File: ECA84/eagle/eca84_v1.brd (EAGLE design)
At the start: 223 x 127 mm, 184 parts

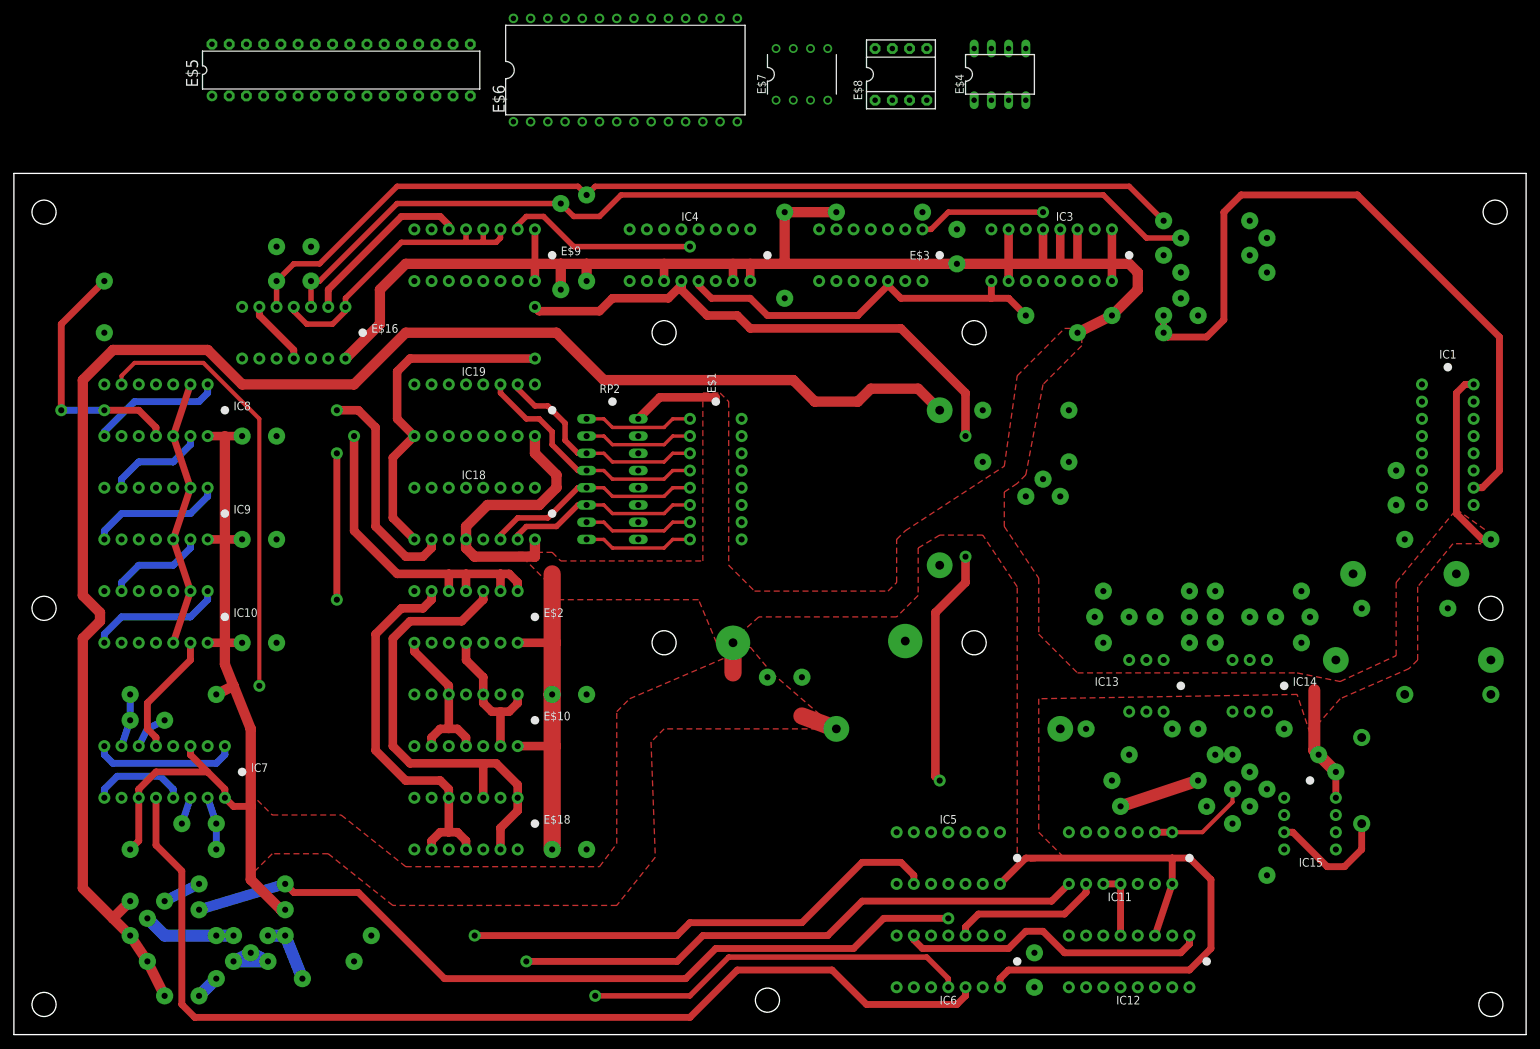
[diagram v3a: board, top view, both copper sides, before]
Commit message: Creando polígonos bottom
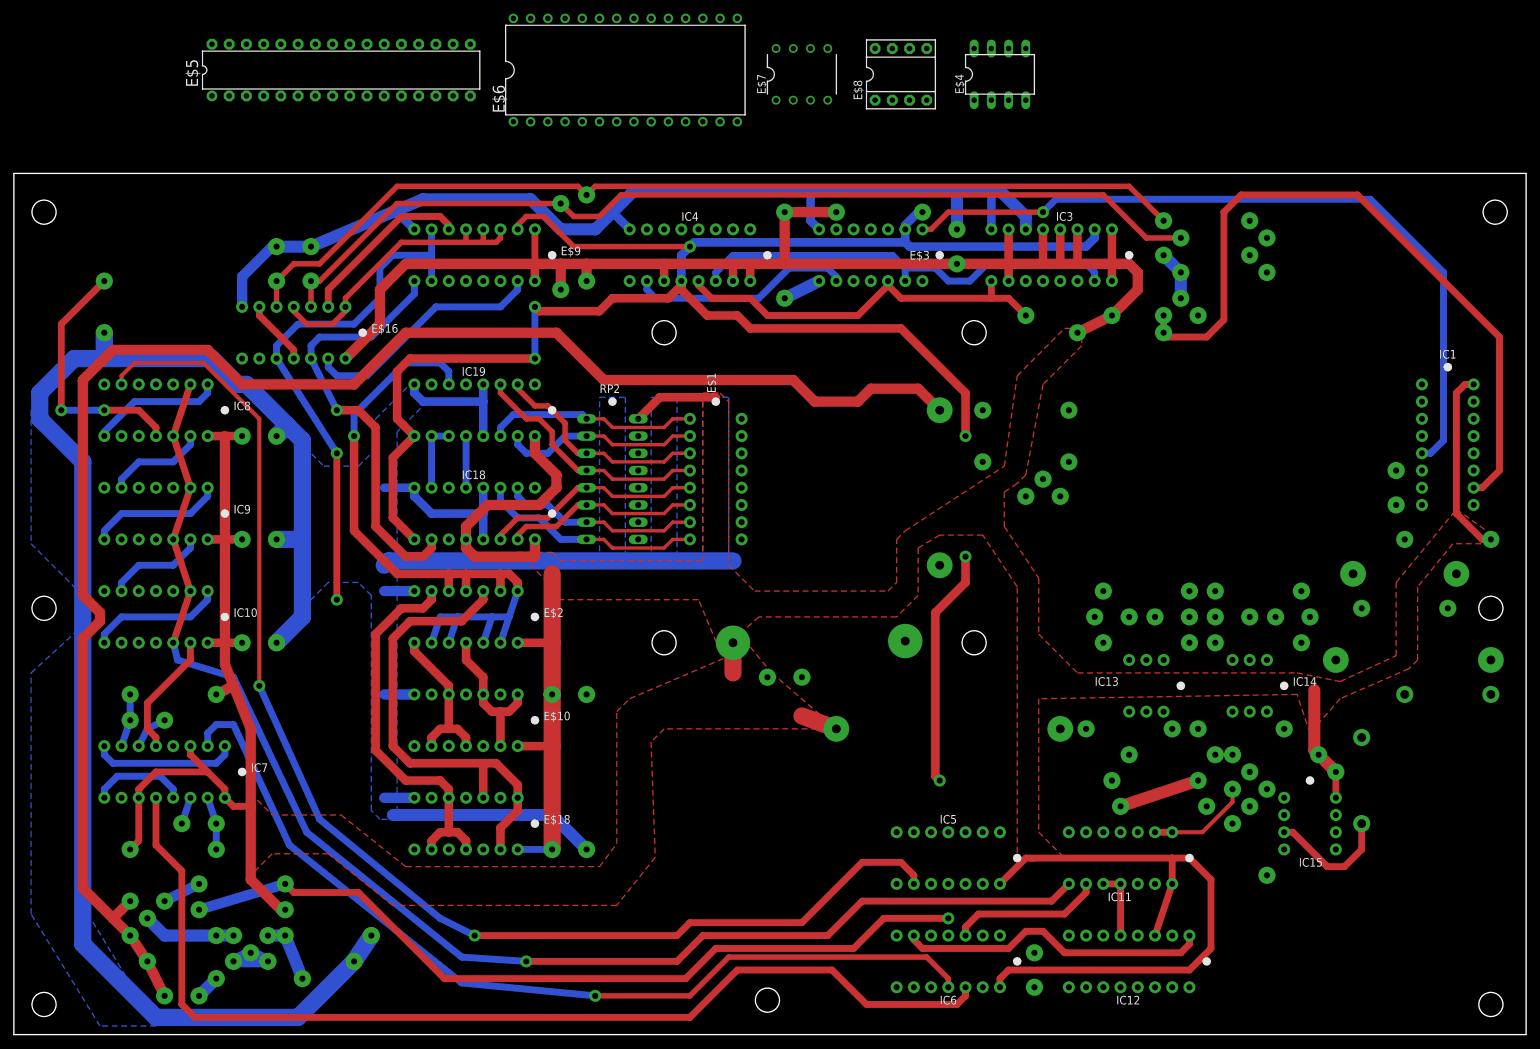
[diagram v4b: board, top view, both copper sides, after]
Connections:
- removed net S$63: E$12.P$1, E$21.P$1, E$23.P$1, E$25.P$1, E$50.P$1, E$51.P$1, IC8.P$7
- new net GND: E$10.P$7, E$12.P$1, E$18.P$7, E$2.P$7, E$21.P$1, E$23.P$1, E$25.P$1, E$50.P$1, E$51.P$1, E$92.P$1, IC18.P$13, IC18.P$4, IC18.P$8, IC19.P$13, IC19.P$4, IC19.P$8, IC8.P$7
- new net S$1: E$10.P$1, E$10.P$13, E$10.P$3, E$2.P$11
- new net S$14: E$103.P$1, E$117.P$1, E$143.P$1, E$161.P$1, E$163.P$1, E$77.P$1, IC1.P$8, IC1.P$9, IC13.P$4, IC5.P$7, IC6.P$7
- new net S$19: IC18.P$7, IC19.P$10, IC19.P$11
- new net S$20: E$74.P$1, E$75.P$1, E$76.P$1
- new net S$21: IC5.P$10, IC6.P$13, IC6.P$2, IC6.P$4
- new net S$25: IC5.P$8, IC6.P$5
- new net S$3: E$3.P$13, IC3.P$15, IC4.P$14
- new net S$36: E$14.P$1
- new net S$41: IC18.P$5, IC19.P$12
- net S$22: no longer E$10.P$1, E$10.P$13, E$10.P$3, E$2.P$11
- net S$29: now also IC18.P$2
- net S$31: now also IC19.P$14
- net S$32: now also IC19.P$15
- net S$34: now also IC18.P$3
- net S$42: now also IC1.P$5
- net S$7: now also IC5.P$11
- net VCC: now also E$18.P$14; no longer E$14.P$1
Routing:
- net GND: track 0.00 -> 363.3 mm
- net S$64: track 0.00 -> 156.5 mm
- net S$42: track 18.8 -> 111.9 mm
- net S$65: track 157.2 -> 238.3 mm
- net S$9: track 57.0 -> 135.2 mm
- net S$35: track 124.9 -> 200.3 mm
- net S$3: track 0.00 -> 64.5 mm
- net S$69: track 21.6 -> 78.7 mm
- net S$5: track 136.5 -> 186.8 mm
- net S$68: track 0.00 -> 36.3 mm
- net S$66: track 0.00 -> 32.7 mm
- net S$24: track 33.3 -> 64.0 mm
- net S$22: track 72.6 -> 103.1 mm
- net S$1: track 0.00 -> 22.4 mm
- net S$34: track 16.3 -> 33.3 mm
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- added copper zone on layer 16, net GND

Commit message: todos los conectores en lbr y pcb
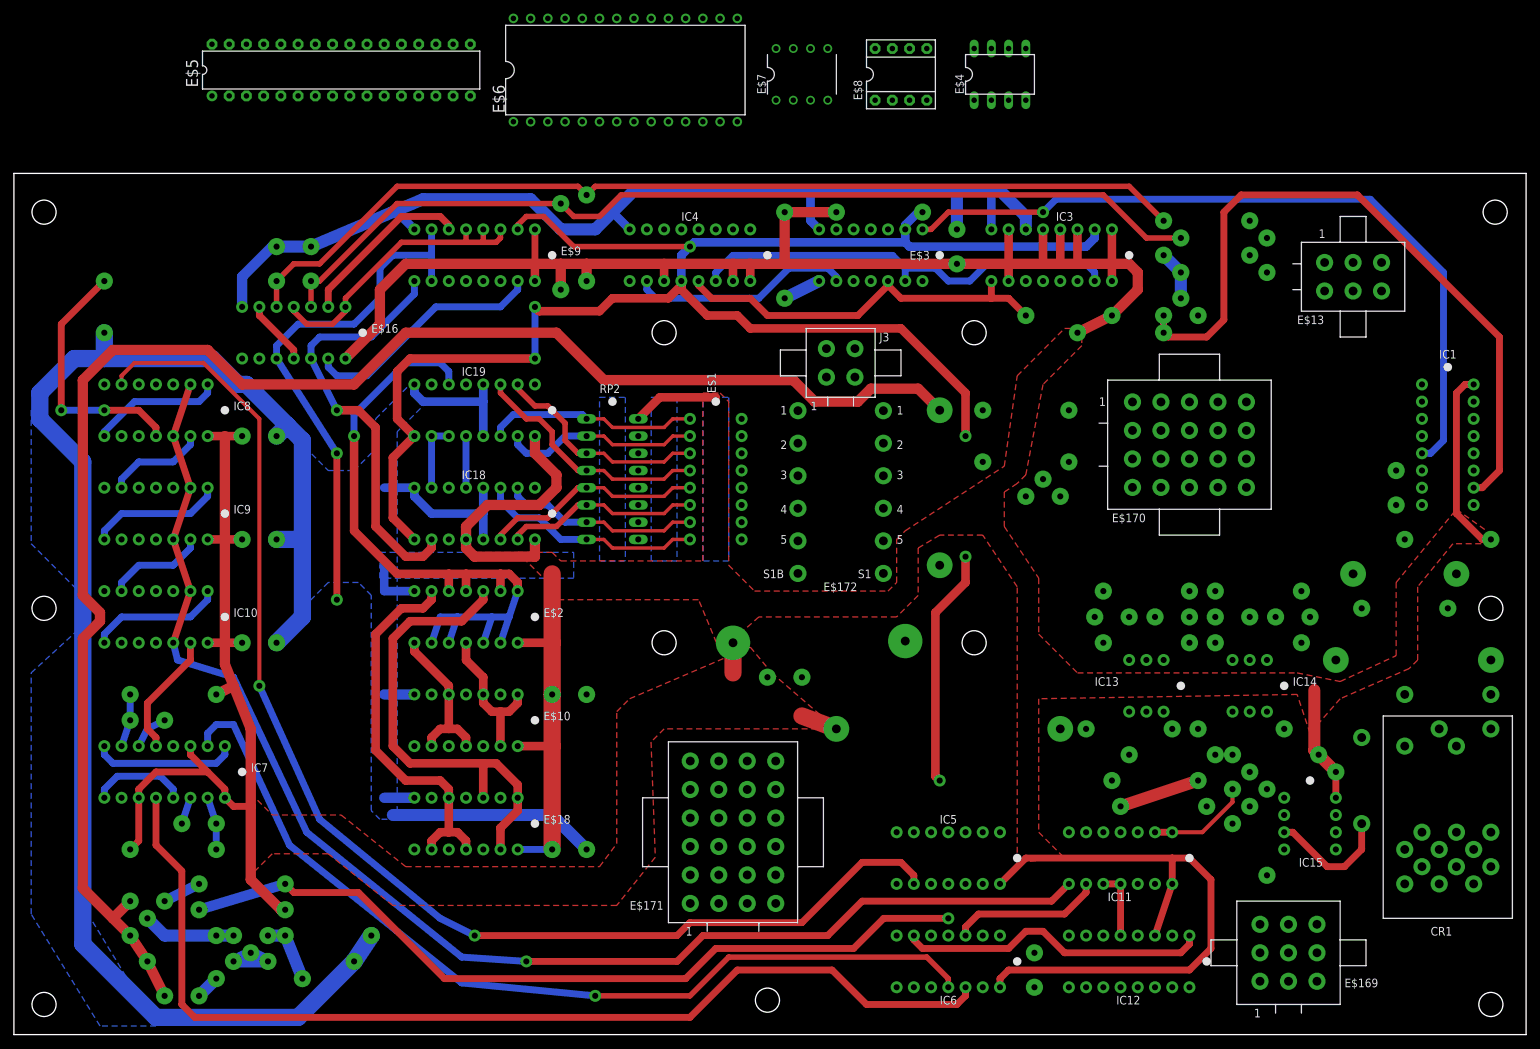
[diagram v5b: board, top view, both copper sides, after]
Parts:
- added CR1: (no value), eca84:CON-ZIGZAG
- added E$13: (no value), eca84:CON-2X3
- added E$169: (no value), eca84:CON-3X3
- added E$170: (no value), eca84:CON-4X5
- added E$171: (no value), eca84:CON-4X6
- added E$172: (no value), eca84:CON-2X6
- added J3: (no value), eca84:CON-2X2
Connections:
- new net S$63: IC18.P$13, IC18.P$4, IC18.P$8, IC19.P$13, IC19.P$4, IC19.P$8
- net GND: no longer IC18.P$13, IC18.P$4, IC18.P$8, IC19.P$13, IC19.P$4, IC19.P$8
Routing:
- net GND: track 363.3 -> 271.3 mm
- net S$63: track 0.00 -> 44.1 mm
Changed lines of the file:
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@@
 <setting verticaltext="up"/>
 </settings>
-<grid distance="25" unitdist="mil" unit="mil" style="lines" multiple="1" display="yes" altdistance="25" altunitdist="mil" altunit="mil"/>
+<grid distance="50" unitdist="mil" unit="mil" style="lines" multiple="1" display="yes" altdistance="25" altunitdist="mil" altunit="mil"/>
 <layers>
-<layer number="1" name="Top" color="4" fill="1" visible="no" active="yes"/>
+<layer number="1" name="Top" color="4" fill="1" visible="yes" active="yes"/>
 <layer number="2" name="Route2" color="16" fill="1" visible="no" active="no"/>
 <layer number="3" name="Route3" color="17" fill="1" visible="no" active="no"/>
@@
 <element name="E$167" library="eca84" package="ROUND-6" value="" x="106.045" y="57.785" smashed="yes"/>
 <element name="E$168" library="eca84" package="ROUND-3" value="" x="113.665" y="108.585" smashed="yes"/>
+<element name="CR1" library="eca84" package="CON-ZIGZAG" value="" x="211.455" y="33.655" smashed="yes">
+<attribute name="NAME" x="208.915" y="14.605" size="1.27" layer="25"/>
+</element>
+<element name="J3" library="eca84" package="CON-2X2" value="" x="121.92" y="99.06" smashed="yes">
+<attribute name="NAME" x="127.635" y="102.235" size="1.27" layer="25"/>
+</element>
+<element name="E$13" library="eca84" package="CON-2X3" value="" x="197.485" y="111.76" smashed="yes">
+<attribute name="NAME" x="189.23" y="104.775" size="1.27" layer="25"/>
+</element>
+<element name="E$169" library="eca84" package="CON-3X3" value="" x="187.96" y="12.065" smashed="yes">
+<attribute name="NAME" x="196.215" y="6.985" size="1.27" layer="25"/>
+</element>
+<element name="E$170" library="eca84" package="CON-4X5" value="" x="173.355" y="86.995" smashed="yes">
+<attribute name="NAME" x="161.925" y="75.565" size="1.27" layer="25"/>
+</element>
+<element name="E$171" library="eca84" package="CON-4X6" value="" x="106.045" y="29.845" smashed="yes">
+<attribute name="NAME" x="90.805" y="18.415" size="1.27" layer="25"/>
+</element>
+<element name="E$172" library="eca84" package="CON-2X6" value="" x="121.92" y="80.01" smashed="yes">
+<attribute name="NAME" x="119.38" y="65.405" size="1.27" layer="25"/>
+</element>
 </elements>
 <signals>
@@
 <wire x1="29.845" y1="8.255" x2="27.305" y2="5.715" width="1.778" layer="16"/>
 </signal>
+<signal name="S$63">
+<contactref element="IC19" pad="P$8"/>
+<wire x1="59.055" y1="94.615" x2="59.055" y2="95.885" width="1.27" layer="16"/>
+<wire x1="60.325" y1="93.345" x2="59.055" y2="94.615" width="1.27" layer="16"/>
+<contactref element="IC19" pad="P$4"/>
+<wire x1="69.215" y1="95.885" x2="69.215" y2="93.345" width="1.27" layer="16"/>
+<wire x1="69.215" y1="93.345" x2="60.325" y2="93.345" width="1.27" layer="16"/>
+<contactref element="IC19" pad="P$13"/>
+<wire x1="69.215" y1="88.265" x2="69.215" y2="93.345" width="1.27" layer="16"/>
+<contactref element="IC18" pad="P$13"/>
+<contactref element="IC18" pad="P$4"/>
+<wire x1="69.215" y1="80.645" x2="69.215" y2="76.835" width="1.27" layer="16"/>
+<wire x1="69.215" y1="76.835" x2="69.215" y2="73.025" width="1.27" layer="16"/>
+<wire x1="61.595" y1="76.835" x2="69.215" y2="76.835" width="1.27" layer="16"/>
+<wire x1="59.055" y1="79.375" x2="61.595" y2="76.835" width="1.27" layer="16"/>
+<contactref element="IC18" pad="P$8"/>
+<wire x1="59.055" y1="80.645" x2="59.055" y2="79.375" width="1.27" layer="16"/>
+<wire x1="54.61" y1="80.645" x2="59.055" y2="80.645" width="1.27" layer="16"/>
+<wire x1="69.215" y1="80.645" x2="69.215" y2="88.265" width="0" layer="19" extent="1-1"/>
+</signal>
 <signal name="GND">
 <contactref element="E$50" pad="P$1"/>
@@
 <wire x1="3.81" y1="94.615" x2="3.81" y2="90.805" width="2.54" layer="16"/>
 <wire x1="52.705" y1="14.605" x2="50.165" y2="10.795" width="2.54" layer="16"/>
-<contactref element="E$18" pad="P$7"/>
-<contactref element="E$92" pad="P$1"/>
-<contactref element="E$10" pad="P$7"/>
-<contactref element="E$2" pad="P$7"/>
-<contactref element="IC19" pad="P$8"/>
-<contactref element="IC19" pad="P$4"/>
-<contactref element="IC19" pad="P$13"/>
 <polygon width="0.254" layer="16" thermals="no">
 <vertex x="41.91" y="87.63"/>
-<vertex x="45.72" y="83.82"/>
-<vertex x="50.8" y="83.82"/>
+<vertex x="46.355" y="83.185"/>
+<vertex x="50.165" y="83.185"/>
 <vertex x="53.34" y="86.36"/>
 <vertex x="53.34" y="90.805"/>
@@
 <vertex x="2.54" y="53.34"/>
 </polygon>
-<wire x1="59.055" y1="50.165" x2="54.61" y2="50.165" width="1.524" layer="16"/>
-<wire x1="59.055" y1="65.405" x2="54.61" y2="65.405" width="1.524" layer="16"/>
-<wire x1="59.055" y1="34.925" x2="54.61" y2="34.925" width="1.524" layer="16"/>
-<contactref element="IC18" pad="P$4"/>
-<contactref element="IC18" pad="P$13"/>
-<contactref element="IC18" pad="P$8"/>
-<wire x1="69.215" y1="80.645" x2="69.215" y2="76.835" width="1.27" layer="16"/>
-<wire x1="69.215" y1="76.835" x2="69.215" y2="73.025" width="1.27" layer="16"/>
-<wire x1="59.055" y1="80.645" x2="59.055" y2="79.375" width="1.27" layer="16"/>
-<wire x1="59.055" y1="79.375" x2="61.595" y2="76.835" width="1.27" layer="16"/>
-<wire x1="61.595" y1="76.835" x2="69.215" y2="76.835" width="1.27" layer="16"/>
-<wire x1="59.055" y1="80.645" x2="54.61" y2="80.645" width="1.27" layer="16"/>
-<wire x1="69.215" y1="95.885" x2="69.215" y2="93.345" width="1.27" layer="16"/>
-<wire x1="69.215" y1="88.265" x2="69.215" y2="93.345" width="1.27" layer="16"/>
-<wire x1="69.215" y1="93.345" x2="60.325" y2="93.345" width="1.27" layer="16"/>
-<wire x1="60.325" y1="93.345" x2="59.055" y2="94.615" width="1.27" layer="16"/>
-<wire x1="59.055" y1="94.615" x2="59.055" y2="95.885" width="1.27" layer="16"/>
-<wire x1="84.455" y1="27.305" x2="79.375" y2="32.385" width="1.778" layer="16"/>
-<wire x1="79.375" y1="32.385" x2="55.88" y2="32.385" width="1.778" layer="16"/>
-<polygon width="0.254" layer="16">
+<polygon width="0.254" layer="16" thermals="no">
 <vertex x="86.36" y="93.98"/>
 <vertex x="90.17" y="93.98"/>
@@
 <vertex x="86.36" y="69.85"/>
 </polygon>
-<polygon width="0.254" layer="16">
+<polygon width="0.254" layer="16" thermals="no">
 <vertex x="93.98" y="93.98"/>
 <vertex x="97.79" y="93.98"/>
@@
 <vertex x="93.98" y="69.85"/>
 </polygon>
-<polygon width="0.254" layer="16">
+<polygon width="0.254" layer="16" thermals="no">
 <vertex x="101.6" y="93.98"/>
 <vertex x="105.41" y="93.98"/>
@@
 <vertex x="101.6" y="69.85"/>
 </polygon>
-<wire x1="54.61" y1="69.215" x2="55.245" y2="69.85" width="2.54" layer="16"/>
-<wire x1="55.245" y1="69.85" x2="106.045" y2="69.85" width="2.54" layer="16"/>
+<contactref element="E$92" pad="P$1"/>
+<contactref element="E$2" pad="P$7"/>
+<wire x1="59.055" y1="65.405" x2="54.61" y2="65.405" width="1.27" layer="16"/>
+<contactref element="E$10" pad="P$7"/>
+<wire x1="59.055" y1="50.165" x2="54.61" y2="50.165" width="1.524" layer="16"/>
+<wire x1="84.455" y1="27.305" x2="79.375" y2="32.385" width="1.778" layer="16"/>
+<wire x1="79.375" y1="32.385" x2="55.88" y2="32.385" width="1.778" layer="16"/>
+<contactref element="E$18" pad="P$7"/>
+<wire x1="59.055" y1="34.925" x2="54.61" y2="34.925" width="1.524" layer="16"/>
+<polygon width="0.254" layer="16" thermals="no">
+<vertex x="53.975" y="71.12"/>
+<vertex x="82.55" y="71.12"/>
+<vertex x="82.55" y="67.31"/>
+<vertex x="53.975" y="67.31"/>
+</polygon>
+<wire x1="54.61" y1="65.405" x2="54.61" y2="69.215" width="1.27" layer="16"/>
 <wire x1="13.335" y1="103.505" x2="13.335" y2="95.885" width="0" layer="19" extent="1-1"/>
 </signal>

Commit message: terminado pistas top
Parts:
- removed E$4: (no value), 40xx:DIL08
- removed E$5: (no value), am29-memory:DIL32-3
- removed E$6: (no value), analog-devices:DIL28-6
- removed E$7: (no value), avago:DIL08
- removed E$8: (no value), burr-brown:DIL08
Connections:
- new net S$70: E$1.P$11, E$172.P$4
- new net S$71: E$1.P$10, E$172.P$6
- new net S$72: E$1.P$9, E$172.P$10
- new net S$73: E$141.P$1, E$170.P$9
- new net S$74: E$140.P$1, E$170.P$13
- new net S$75: E$13.P$2, E$170.P$17
- new net S$76: E$13.P$1, E$170.P$14
- new net S$77: E$170.P$10, E$85.P$1
- new net S$78: E$170.P$11, E$89.P$1
- new net S$79: E$13.P$3, E$162.P$1
- net S$36: now also E$1.P$12, E$172.P$2; no longer E$14.P$1
- net VCC: now also E$14.P$1, IC1.P$11
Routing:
- net S$79: track 0.00 -> 47.6 mm
- net S$74: track 0.00 -> 37.0 mm
- net S$73: track 0.00 -> 30.4 mm
- net S$76: track 0.00 -> 30.2 mm
- net S$70: track 0.00 -> 24.7 mm
- net S$71: track 0.00 -> 24.1 mm
- net S$72: track 0.00 -> 23.0 mm
- net S$78: track 0.00 -> 21.3 mm
- net S$36: track 5.43 -> 25.6 mm
- net S$75: track 0.00 -> 20.0 mm
- net S$77: track 0.00 -> 19.0 mm
- net VCC: track 491.7 -> 499.6 mm

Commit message: Antes de cambiar angulo de pistas
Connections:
- new net S$80: E$10.P$6, E$171.P$20
- new net S$81: E$10.P$4, E$171.P$24
- new net S$82: E$10.P$2, E$171.P$16
- new net S$83: E$10.P$10, E$171.P$17
- new net S$84: E$10.P$12, E$171.P$13
- new net S$85: E$10.P$8, E$171.P$21
- new net S$86: E$171.P$12, E$18.P$12
- new net S$87: E$171.P$9, E$18.P$6
- new net S$88: E$171.P$5, E$18.P$4
- new net S$89: E$171.P$1, E$18.P$2
- new net S$90: E$171.P$4, E$18.P$10
- new net S$91: E$171.P$8, E$18.P$8
- net GND: now also E$171.P$10, E$171.P$11, E$171.P$14, E$171.P$15, E$171.P$18, E$171.P$19, E$171.P$2, E$171.P$22, E$171.P$23, E$171.P$3, E$171.P$6, E$171.P$7, E$94.P$1
- net S$69: now also IC15.P$2, IC6.P$1
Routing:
- net S$69: track 78.7 -> 235.2 mm
- net S$91: track 0.00 -> 74.9 mm
- net S$80: track 0.00 -> 70.2 mm
- net S$86: track 0.00 -> 59.9 mm
- net S$90: track 0.00 -> 59.1 mm
- net GND: track 271.3 -> 328.4 mm
- net S$81: track 0.00 -> 56.2 mm
- net S$82: track 0.00 -> 56.2 mm
- net S$87: track 0.00 -> 46.6 mm
- net S$85: track 0.00 -> 46.6 mm
- net S$88: track 0.00 -> 42.2 mm
- net S$83: track 0.00 -> 42.2 mm
- net S$84: track 0.00 -> 37.8 mm
- net S$89: track 0.00 -> 37.3 mm
